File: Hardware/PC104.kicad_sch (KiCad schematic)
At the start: 0 parts

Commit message: Add PC104 header sub-schematic
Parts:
- added C1, C3, C4: 4.7uF, symbol Device:C_Polarized
- added J1, J2: ESQ-126-14-G-D, ESQ-126-14-G-D:SAMTEC_ESQ-126-14-G-D, symbol ESQ-126-14-G-D:ESQ-126-14-G-D
- added R10, R11, R12, R13, R14, R15, R16, R17, R18, R19, R20, R21, R22, R23, R24, R25, R26, R27, R28, R29, R3, R30, R31, R32, R33, R34, R35, R36, R37, R4, R5, R6, R7, R8, R9: 100K, symbol Device:R_US
- added R38, R39: 10K, symbol Device:R_US
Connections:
- new net: J1.26, J1.30, R13.1
- new net: J2.21, R20.2
- new net: J1.44, R11.1
- new net: J1.12, R17.1
- new net: J1.33, J1.35, J1.37, R3.2
- new net: J2.16, R28.1
- new net: J2.52, R37.1
- new net: J2.17, R22.2
- new net: J2.01, J2.03, J2.05, J2.07, J2.09, J2.11, J2.13, R33.2
- new net: J2.02, J2.04, J2.06, J2.08, J2.10, J2.12, J2.14, R34.2
- new net: J2.15, R23.2
- new net: J2.18, R27.1
- new net: J2.19, R21.2
- new net: J2.20, R26.1
- new net: J2.22, R25.1
- new net: J2.23, R19.2
- new net: J2.24, R24.1
- new net: J2.31, R32.2
- new net: J2.33, J2.35, J2.37, R31.2
- new net: J2.34, J2.36, J2.38, R35.2
- new net: J2.47, R30.2
- new net: J2.48, R36.1
- new net: J2.49, R29.2
- new net: J1.14, R16.1
- new net: J1.16, R15.1
- new net: J1.18, J1.20, R14.1
- new net: J1.03, R8.2
- new net: J1.01, R9.2
- new net: J1.10, R18.1
- new net: J1.13, R7.2
- new net: J1.15, R6.2
- new net: J1.17, J1.19, R5.2
- new net: J1.25, J1.29, R4.2
- new net: J1.36, R12.1
- new net: J1.46, R10.1
- new net +3V3: J2.27, J2.28
- new net +5V: C1.1, J2.25, J2.26
- new net 3V3_ANT_DEPLOY: C4.1, J1.50
- new net 3V3_CAM: C3.1, J1.48
- new net 5V0_MPI: J1.51
- new net GND: C1.2, C3.2, C4.2, J1.22, J1.24, J1.27, J1.28, J1.31, J1.32, J1.39, J1.40, J1.42, J2.29, J2.30, J2.32, J2.39, J2.40, J2.41, J2.42, J2.43, J2.44, R10.2, R11.2, R12.2, R13.2, R14.2, R15.2, R16.2, R17.2, R18.2, R19.1, R20.1, R21.1, R22.1, R23.1, R24.2, R25.2, R26.2, R27.2, R28.2, R29.1, R3.1, R30.1, R31.1, R32.1, R33.1, R34.1, R35.1, R36.2, R37.2, R39.2, R4.1, R5.1, R6.1, R7.1, R8.1, R9.1
- new net I2C1_SCL: J1.43
- new net I2C1_SDA: J1.41
- new net VBAT_MONITOR: R38.2, R39.1
- new net V_BAT: J2.45, J2.46, R38.1
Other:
- note added: "H1"
- note added: "H2"

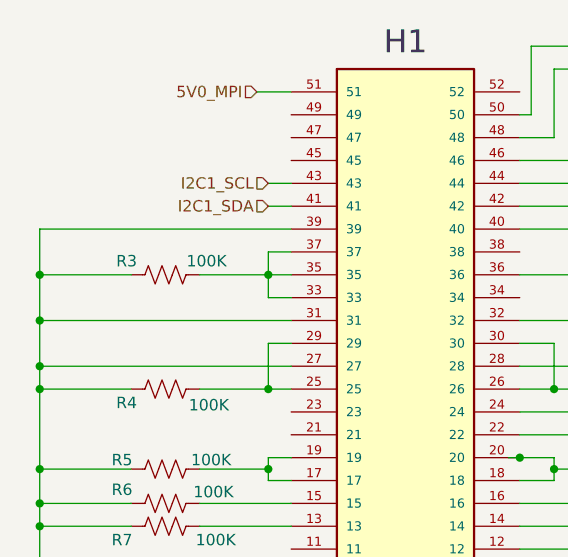
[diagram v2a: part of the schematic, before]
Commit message: Add STM32 I2C and SPI connections
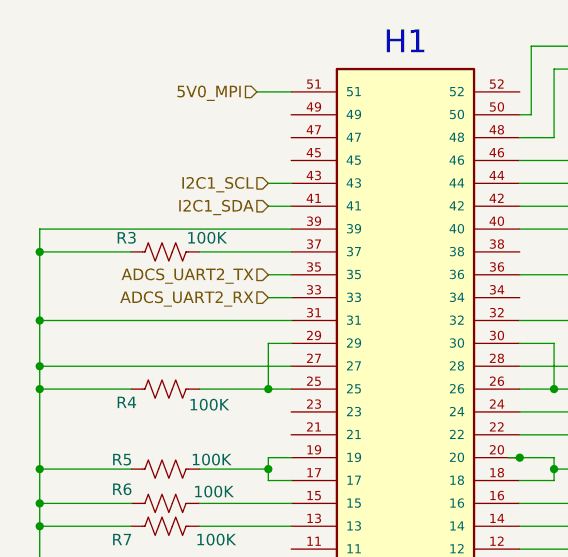
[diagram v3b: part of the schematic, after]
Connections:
- net at J1.37, R3.2: no longer J1.33, J1.35
- new net ADCS_UART2_RX: J1.33
- new net ADCS_UART2_TX: J1.35
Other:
- moved on the sheet: R3
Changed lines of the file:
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@@
-	)
-	(junction
-		(at 125.73 78.74)
-		(diameter 0)
-		(color 0 0 0 0)
 	)
 	(junction
@@
 	)
 	(junction
-		(at 151.13 78.74)
-		(diameter 0)
-		(color 0 0 0 0)
-	)
-	(junction
 		(at 151.13 100.33)
 		(diameter 0)
@@
 	)
 	(junction
+		(at 125.73 76.2)
+		(diameter 0)
+		(color 0 0 0 0)
+	)
+	(junction
 		(at 207.01 190.5)
 		(diameter 0)
@@
 	(wire
 		(pts
-			(xy 153.67 81.28) (xy 151.13 81.28)
-		)
-		(stroke
-			(width 0)
-			(type default)
-		)
-	)
-	(wire
-		(pts
 			(xy 179.07 160.02) (xy 207.01 160.02)
 		)
@@
 	(wire
 		(pts
-			(xy 151.13 81.28) (xy 151.13 78.74)
-		)
-		(stroke
-			(width 0)
-			(type default)
-		)
-	)
-	(wire
-		(pts
 			(xy 212.09 66.04) (xy 212.09 64.77)
 		)
@@
 	(wire
 		(pts
-			(xy 143.51 78.74) (xy 151.13 78.74)
-		)
-		(stroke
-			(width 0)
-			(type default)
-		)
-	)
-	(wire
-		(pts
 			(xy 207.01 66.04) (xy 207.01 68.58)
 		)
@@
 	(wire
 		(pts
-			(xy 125.73 73.66) (xy 125.73 78.74)
+			(xy 125.73 73.66) (xy 125.73 76.2)
 		)
 		(stroke
@@
 	(wire
 		(pts
+			(xy 125.73 76.2) (xy 125.73 83.82)
+		)
+		(stroke
+			(width 0)
+			(type default)
+		)
+	)
+	(wire
+		(pts
 			(xy 181.61 205.74) (xy 181.61 203.2)
 		)
@@
 	(wire
 		(pts
-			(xy 135.89 78.74) (xy 125.73 78.74)
+			(xy 135.89 76.2) (xy 125.73 76.2)
 		)
 		(stroke
@@
 	(wire
 		(pts
+			(xy 151.13 78.74) (xy 153.67 78.74)
+		)
+		(stroke
+			(width 0)
+			(type default)
+		)
+	)
+	(wire
+		(pts
 			(xy 207.01 172.72) (xy 207.01 175.26)
 		)
@@
 	(wire
 		(pts
+			(xy 151.13 81.28) (xy 153.67 81.28)
+		)
+		(stroke
+			(width 0)
+			(type default)
+		)
+	)
+	(wire
+		(pts
 			(xy 179.07 111.76) (xy 189.23 111.76)
 		)
@@
 	(wire
 		(pts
-			(xy 153.67 76.2) (xy 151.13 76.2)
+			(xy 143.51 76.2) (xy 153.67 76.2)
 		)
 		(stroke
@@
 	(wire
 		(pts
-			(xy 151.13 78.74) (xy 153.67 78.74)
-		)
-		(stroke
-			(width 0)
-			(type default)
-		)
-	)
-	(wire
-		(pts
 			(xy 143.51 119.38) (xy 153.67 119.38)
 		)
@@
 	(wire
 		(pts
-			(xy 151.13 76.2) (xy 151.13 78.74)
-		)
-		(stroke
-			(width 0)
-			(type default)
-		)
-	)
-	(wire
-		(pts
 			(xy 179.07 175.26) (xy 207.01 175.26)
 		)
@@
 		(pts
 			(xy 207.01 106.68) (xy 196.85 106.68)
-		)
-		(stroke
-			(width 0)
-			(type default)
-		)
-	)
-	(wire
-		(pts
-			(xy 125.73 78.74) (xy 125.73 83.82)
 		)
 		(stroke
@@
 		(shape input)
 		(at 224.79 116.84 180)
+		(effects
+			(font
+				(size 1.27 1.27)
+			)
+			(justify right)
+		)
+	)
+	(hierarchical_label "ADCS_UART2_RX"
+		(shape input)
+		(at 151.13 81.28 180)
+		(effects
+			(font
+				(size 1.27 1.27)
+			)
+			(justify right)
+		)
+	)
+	(hierarchical_label "ADCS_UART2_TX"
+		(shape input)
+		(at 151.13 78.74 180)
 		(effects
 			(font
@@
 	(symbol
 		(lib_id "Device:R_US")
-		(at 139.7 78.74 90)
+		(at 139.7 76.2 90)
 		(unit 1)
 		(exclude_from_sim no)
@@
 		(dnp no)
 		(property "Reference" "R3"
-			(at 135.382 77.216 90)
+			(at 135.382 74.676 90)
 			(effects
 				(font
@@
 		)
 		(property "Value" "100K"
-			(at 144.272 77.216 90)
+			(at 144.272 74.676 90)
 			(effects
 				(font
@@
 		)
 		(property "Footprint" ""
-			(at 139.954 77.724 90)
+			(at 139.954 75.184 90)
 			(effects
 				(font
@@
 		)
 		(property "Datasheet" "~"
-			(at 139.7 78.74 0)
+			(at 139.7 76.2 0)
 			(effects
 				(font
@@
 		)
 		(property "Description" "Resistor, US symbol"
-			(at 139.7 78.74 0)
-			(effects
-				(font
+			(at 139.7 76.2 0)
+			(effects
+				(font

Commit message: Small updates
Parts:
- removed R10, R11, R12, R13, R14, R15, R16, R17, R18, R19, R20, R21, R22, R23, R24, R25, R26, R27, R28, R29, R3, R30, R31, R32, R33, R34, R35, R36, R37, R4, R5, R6, R7, R8, R9: 100K, symbol Device:R_US
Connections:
- net at J1.26: no longer J1.30
- net at J1.18: no longer J1.20
- net at J1.17: no longer J1.19
- net at J1.25: no longer J1.29
- now unconnected: J2.01, J2.02, J2.03, J2.04, J2.05, J2.06, J2.07, J2.08, J2.09, J2.10, J2.11, J2.12, J2.13, J2.14, J2.33, J2.34, J2.35, J2.36, J2.37, J2.38

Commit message: RP2040 Schematic
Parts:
- renumbered C3 to C15, C1 to C16, C4 to C17, J1 to J2, J2 to J3, R38 to R50, R39 to R51
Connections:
- net V_BAT renamed +BATT

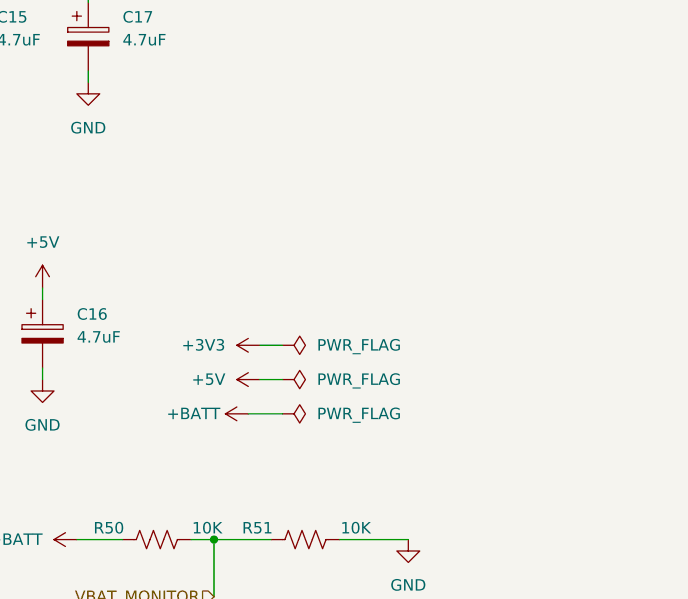
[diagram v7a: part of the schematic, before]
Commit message: Add fast clock
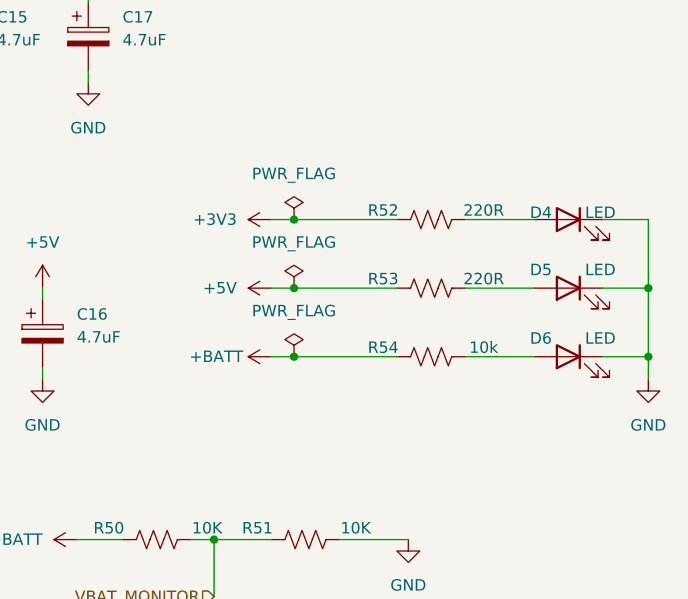
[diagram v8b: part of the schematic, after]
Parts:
- added D4, D5, D6: LED, symbol Device:LED
- added R52, R53: 220R, symbol Device:R_US
- added R54: 10k, symbol Device:R_US
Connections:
- net +3V3: now also R52.1
- net +5V: now also R53.1
- net +BATT: now also R54.1
- net GND: now also D4.1 (K), D5.1 (K), D6.1 (K)
- new net: D4.2 (A), R52.2
- new net: D6.2 (A), R54.2
- new net: D5.2 (A), R53.2
